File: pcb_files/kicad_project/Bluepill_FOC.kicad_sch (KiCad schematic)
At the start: 31 parts, among them J12 Conn_01x05_Pin, J13 Conn_01x05_Pin, J14 Conn_01x05_Pin, J15 Conn_01x05_Pin, J16 Conn_01x05_Pin, J17 Conn_01x03_Pin, J18 Conn_01x03_Pin, Y1 Crystal

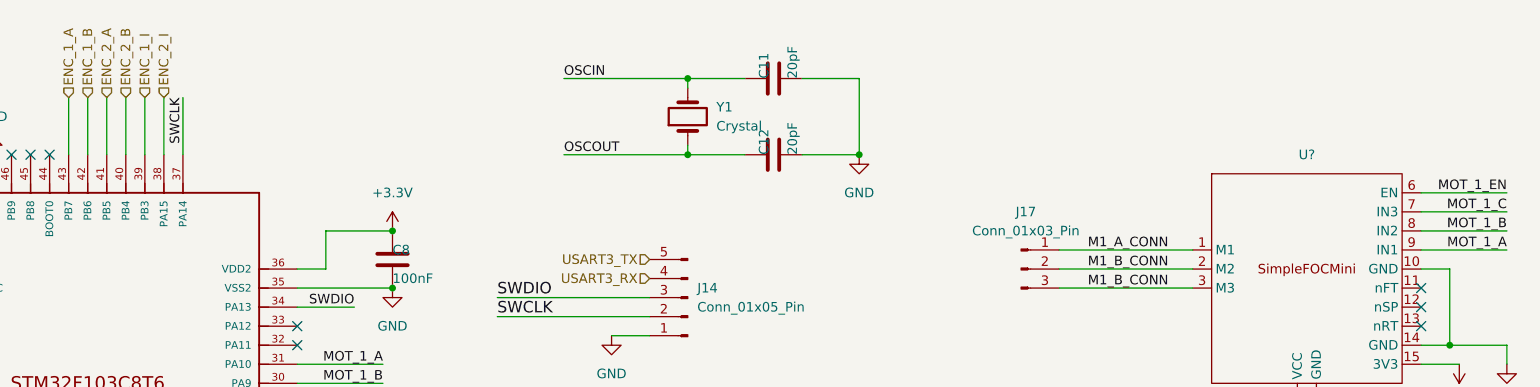
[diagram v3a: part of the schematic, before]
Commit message: Actualiza esquemático e inicia PCB
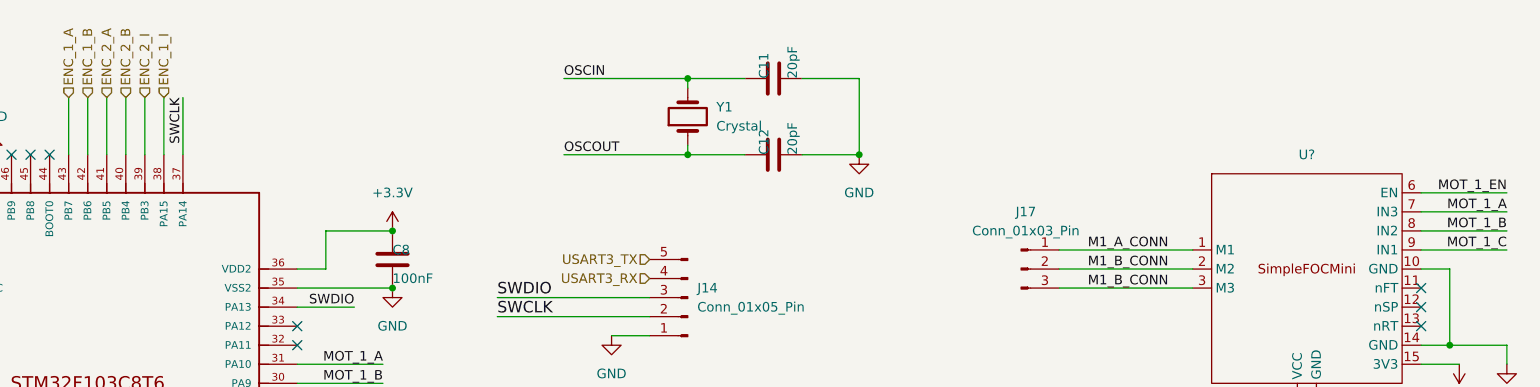
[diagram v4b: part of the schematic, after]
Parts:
- U? (x2): footprint custom_symbols:SimpleFOCMini -> custom_footprints:SimpleFOCMini
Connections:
- net ENC_1_I: now also U?.38 (PA15); no longer U?.39 (PB3)
- net ENC_2_I: now also U?.39 (PB3); no longer U?.38 (PA15)
- net MOT_1_A: now also U?.7 (IN3); no longer U?.9 (IN1)
- net MOT_1_C: now also U?.9 (IN1); no longer U?.7 (IN3)

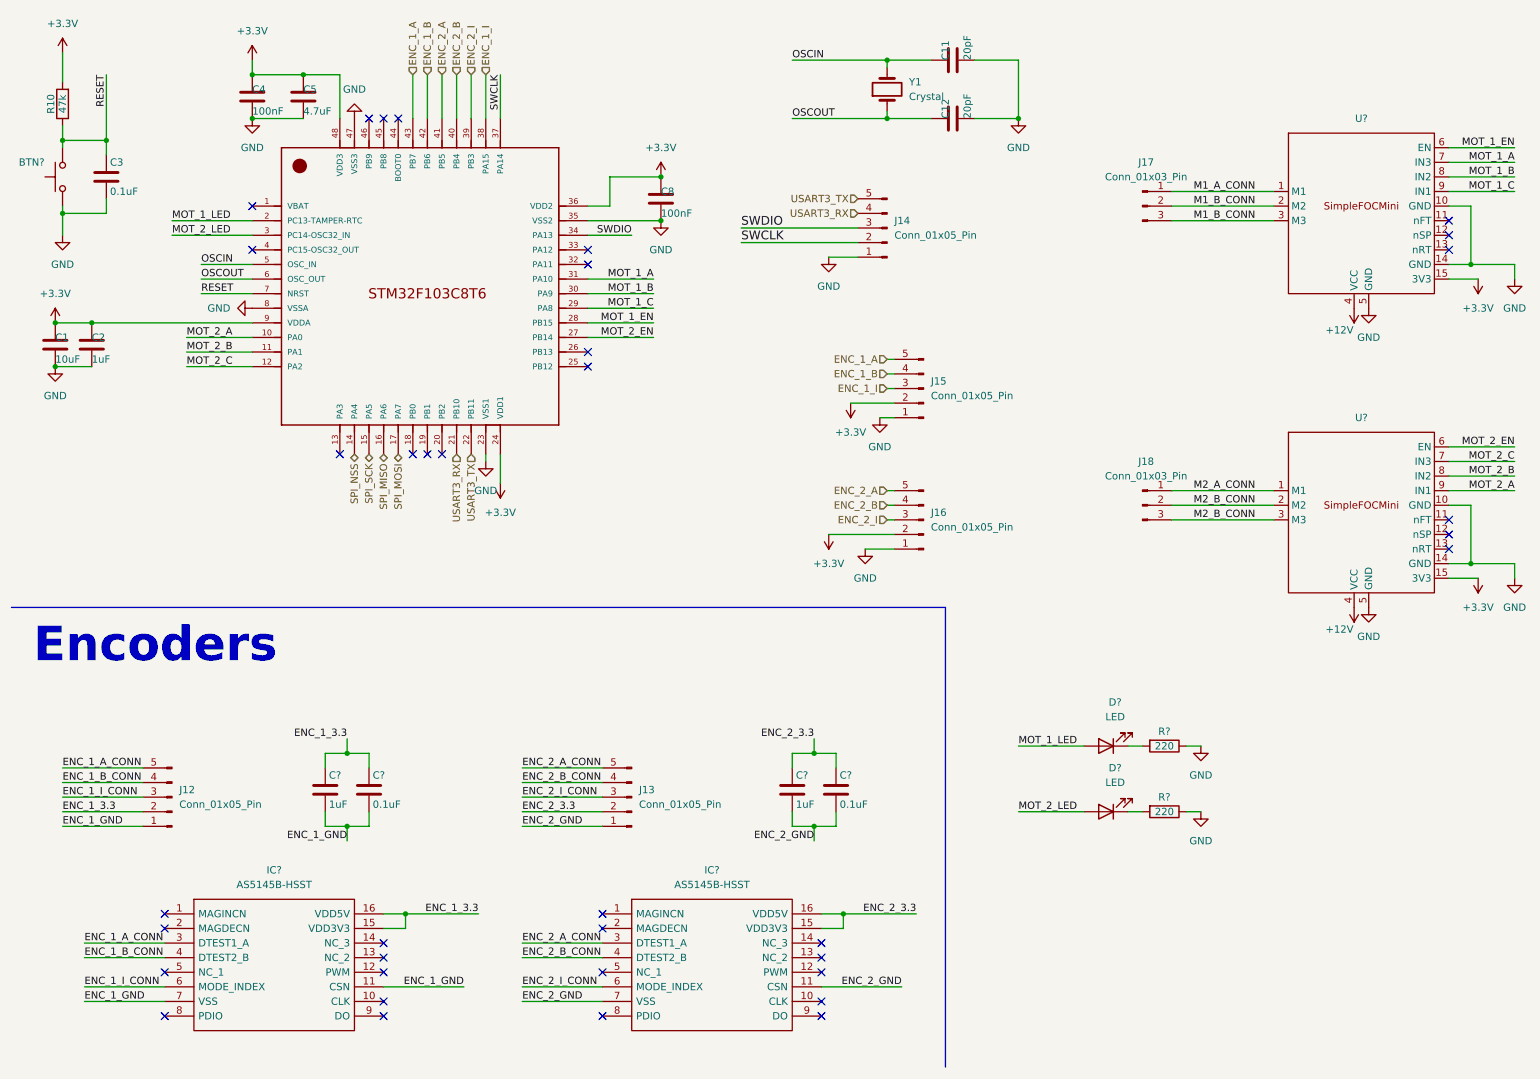
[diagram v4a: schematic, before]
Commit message: Actualiza esquemático y finaliza ruteado de PCB
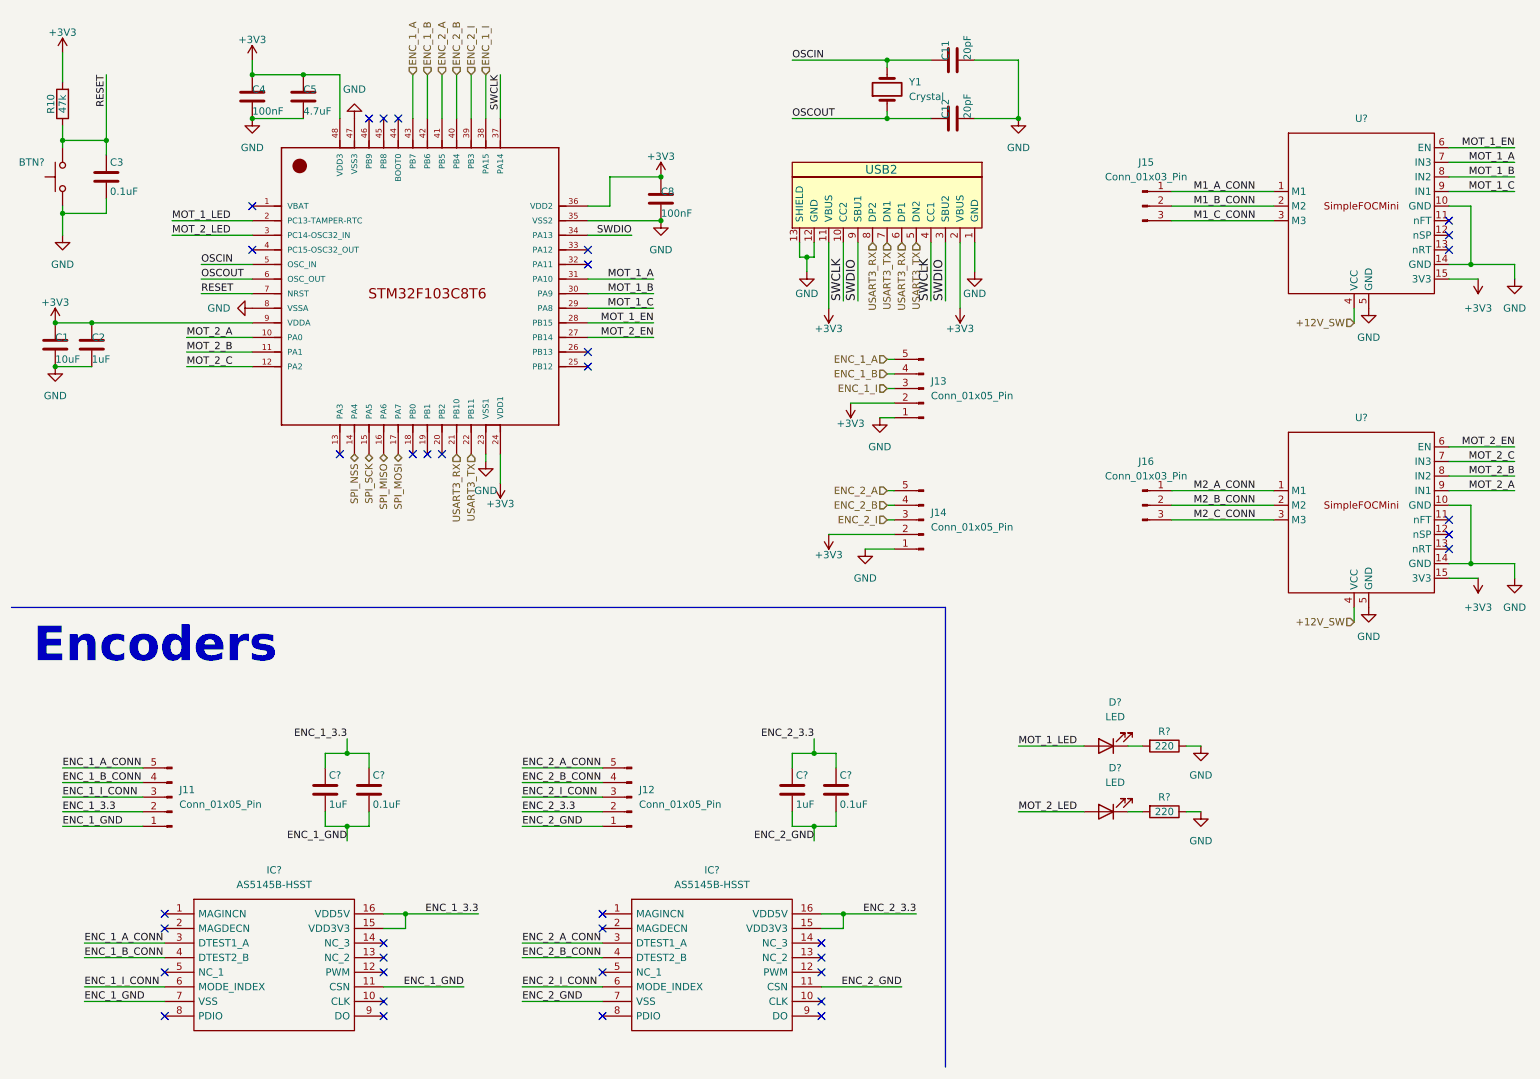
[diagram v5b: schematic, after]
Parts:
- removed J14: Conn_01x05_Pin, Connector_PinHeader_2.54mm:PinHeader_1x05_P2.54mm_Vertical, symbol Connector:Conn_01x05_Pin
- added USB2: ~, custom_footprints:USB-C ST-Link USART, symbol custom_symbols:USB-C_ST-Link_USART
- renumbered J12 to J11, J13 to J12, J15 to J13, J16 to J14, J17 to J15, J18 to J16
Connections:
- net GND: now also USB2.1 (GND), USB2.12 (GND), USB2.13 (SHIELD)
- net M1_B_CONN: no longer J15.3 (Pin_3), U?.3 (M3)
- net M2_B_CONN: no longer J16.3 (Pin_3), U?.3 (M3)
- net SWCLK: now also USB2.10 (CC2), USB2.4 (CC1)
- net SWDIO: now also USB2.3 (SBU2), USB2.9 (SBU1)
- net USART3_RX: now also USB2.6 (DP1), USB2.8 (DP2)
- net USART3_TX: now also USB2.5 (DN2), USB2.7 (DN1)
- net +12V renamed +12V_SW
- net +3.3V renamed +3V3
- net +3V3: now also USB2.11 (VBUS), USB2.2 (VBUS)
- new net M1_C_CONN: J15.3 (Pin_3), U?.3 (M3)
- new net M2_C_CONN: J16.3 (Pin_3), U?.3 (M3)

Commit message: Termina el diseño del esquemático y PCB
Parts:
- J11, J12, J13, J14: footprint Connector_PinHeader_2.54mm:PinHeader_1x05_P2.54mm_Vertical -> custom_footprints:1x05 Pad
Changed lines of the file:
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@@
       (effects (font (size 1.27 1.27)) (justify right))
     )
-    (property "Footprint" "Connector_PinHeader_2.54mm:PinHeader_1x05_P2.54mm_Vertical" (at 40.64 151.13 0)
+    (property "Footprint" "custom_footprints:1x05 Pad" (at 40.64 151.13 0)
       (effects (font (size 1.27 1.27)) hide)
     )
@@
       (effects (font (size 1.27 1.27)) (justify right))
     )
-    (property "Footprint" "Connector_PinHeader_2.54mm:PinHeader_1x05_P2.54mm_Vertical" (at 171.45 80.01 0)
+    (property "Footprint" "custom_footprints:1x05 Pad" (at 171.45 80.01 0)
       (effects (font (size 1.27 1.27)) hide)
     )
@@
       (effects (font (size 1.27 1.27)) (justify right))
     )
-    (property "Footprint" "Connector_PinHeader_2.54mm:PinHeader_1x05_P2.54mm_Vertical" (at 120.65 151.13 0)
+    (property "Footprint" "custom_footprints:1x05 Pad" (at 120.65 151.13 0)
       (effects (font (size 1.27 1.27)) hide)
     )
@@
       (effects (font (size 1.27 1.27)) (justify right))
     )
-    (property "Footprint" "Connector_PinHeader_2.54mm:PinHeader_1x05_P2.54mm_Vertical" (at 171.45 102.87 0)
-      (effects (font (size 1.27 1.27)) hide)
-    )
+    (property "Footprint" "custom_footprints:1x05 Pad" (at 171.45 102.87 0)
+      (effects (font (size 1.27 1.27)) hide)
+    )

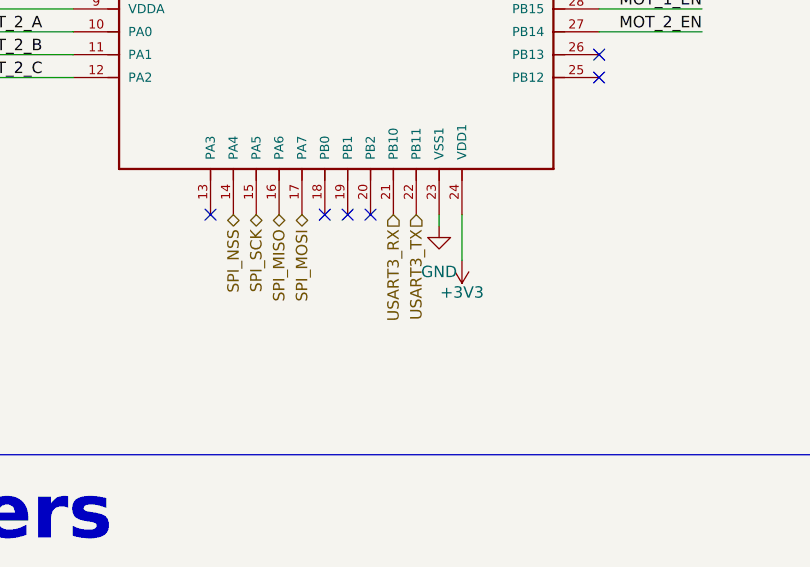
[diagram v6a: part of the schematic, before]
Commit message: Corrige USART6 RX<>TX en la BluePill
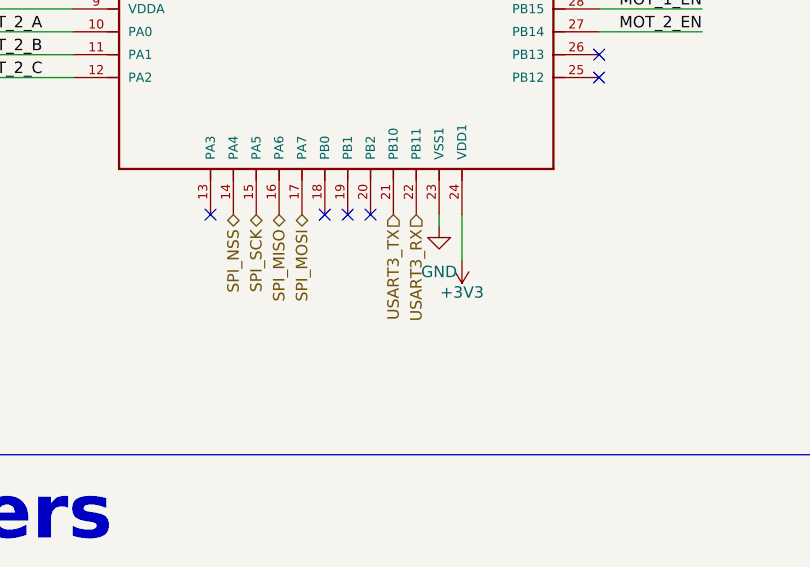
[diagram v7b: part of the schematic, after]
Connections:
- net USART3_RX: now also U?.22 (PB11); no longer U?.21 (PB10)
- net USART3_TX: now also U?.21 (PB10); no longer U?.22 (PB11)
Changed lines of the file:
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@@
     (effects (font (size 1.27 1.27)) (justify left))
-  )
-  (hierarchical_label "USART3_TX" (shape input) (at 92.71 91.44 270) (fields_autoplaced)
-    (effects (font (size 1.27 1.27)) (justify right))
   )
   (hierarchical_label "SPI_MOSI" (shape bidirectional) (at 80.01 91.44 270) (fields_autoplaced)
@@
     (effects (font (size 1.27 1.27)) (justify left))
   )
+  (hierarchical_label "USART3_RX" (shape input) (at 92.71 91.44 270) (fields_autoplaced)
+    (effects (font (size 1.27 1.27)) (justify right))
+  )
   (hierarchical_label "USART3_TX" (shape input) (at 165.1 54.61 270) (fields_autoplaced)
     (effects (font (size 1.27 1.27)) (justify right))
@@
     (effects (font (size 1.27 1.27)) (justify left))
   )
-  (hierarchical_label "USART3_RX" (shape input) (at 90.17 91.44 270) (fields_autoplaced)
+  (hierarchical_label "USART3_TX" (shape input) (at 90.17 91.44 270) (fields_autoplaced)
     (effects (font (size 1.27 1.27)) (justify right))
   )
